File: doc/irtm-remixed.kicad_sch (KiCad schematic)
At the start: 15 parts, among them J1 1x4, right angle pin header, Q1 S8550, Q2 S8550, U1 STC8G1K08A-36I-SOP8, U2 CHQ1838

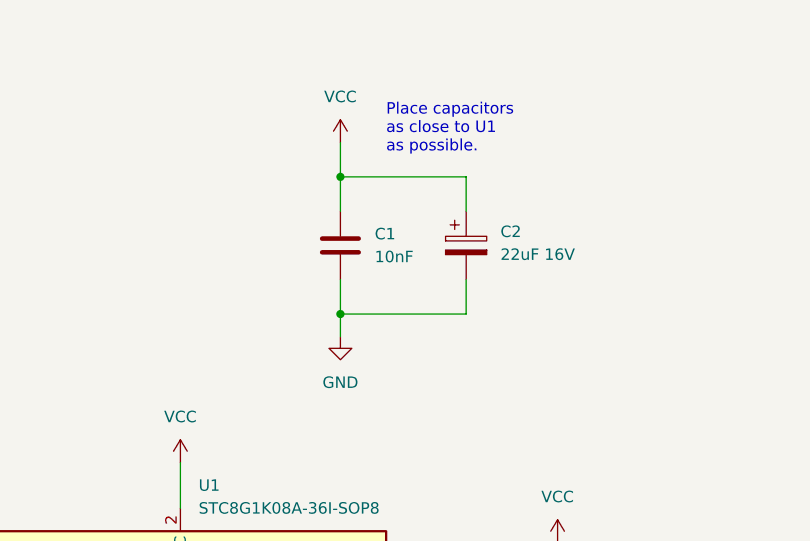
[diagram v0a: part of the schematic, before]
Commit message: Fixed C1's value
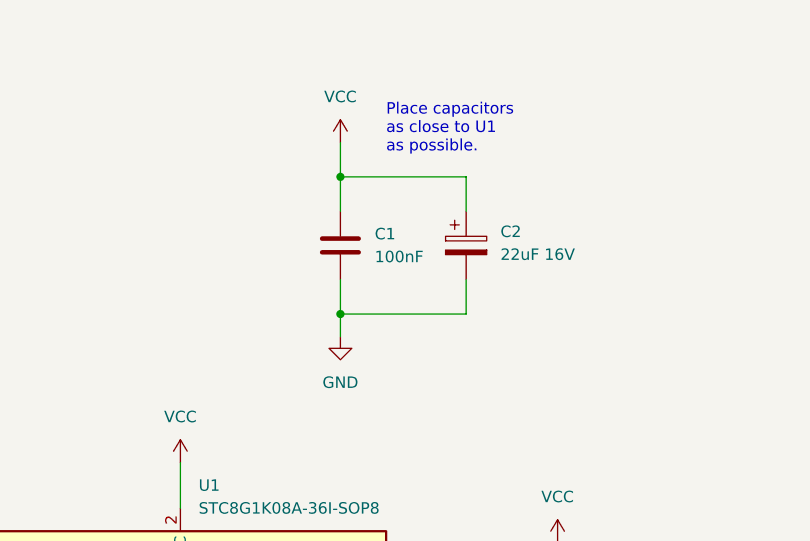
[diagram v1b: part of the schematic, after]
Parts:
- C1: value 10nF -> 100nF
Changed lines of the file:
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@@
       (effects (font (size 1.27 1.27)) (justify left))
     )
-    (property "Value" "10nF" (at 181.61 66.0399 0)
+    (property "Value" "100nF" (at 181.61 66.0399 0)
       (effects (font (size 1.27 1.27)) (justify left))
     )
